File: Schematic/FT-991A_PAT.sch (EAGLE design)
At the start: 51 parts, among them Q1 PE4259, Q10 PE4259, Q2 MC78L09ABDR2GOSCT, Q3 SN74AHC-OR, Q4 PE4259, Q5 NCP553, Q6 PE4259, Q7 J310, Q8 5086, Q9 PE4259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

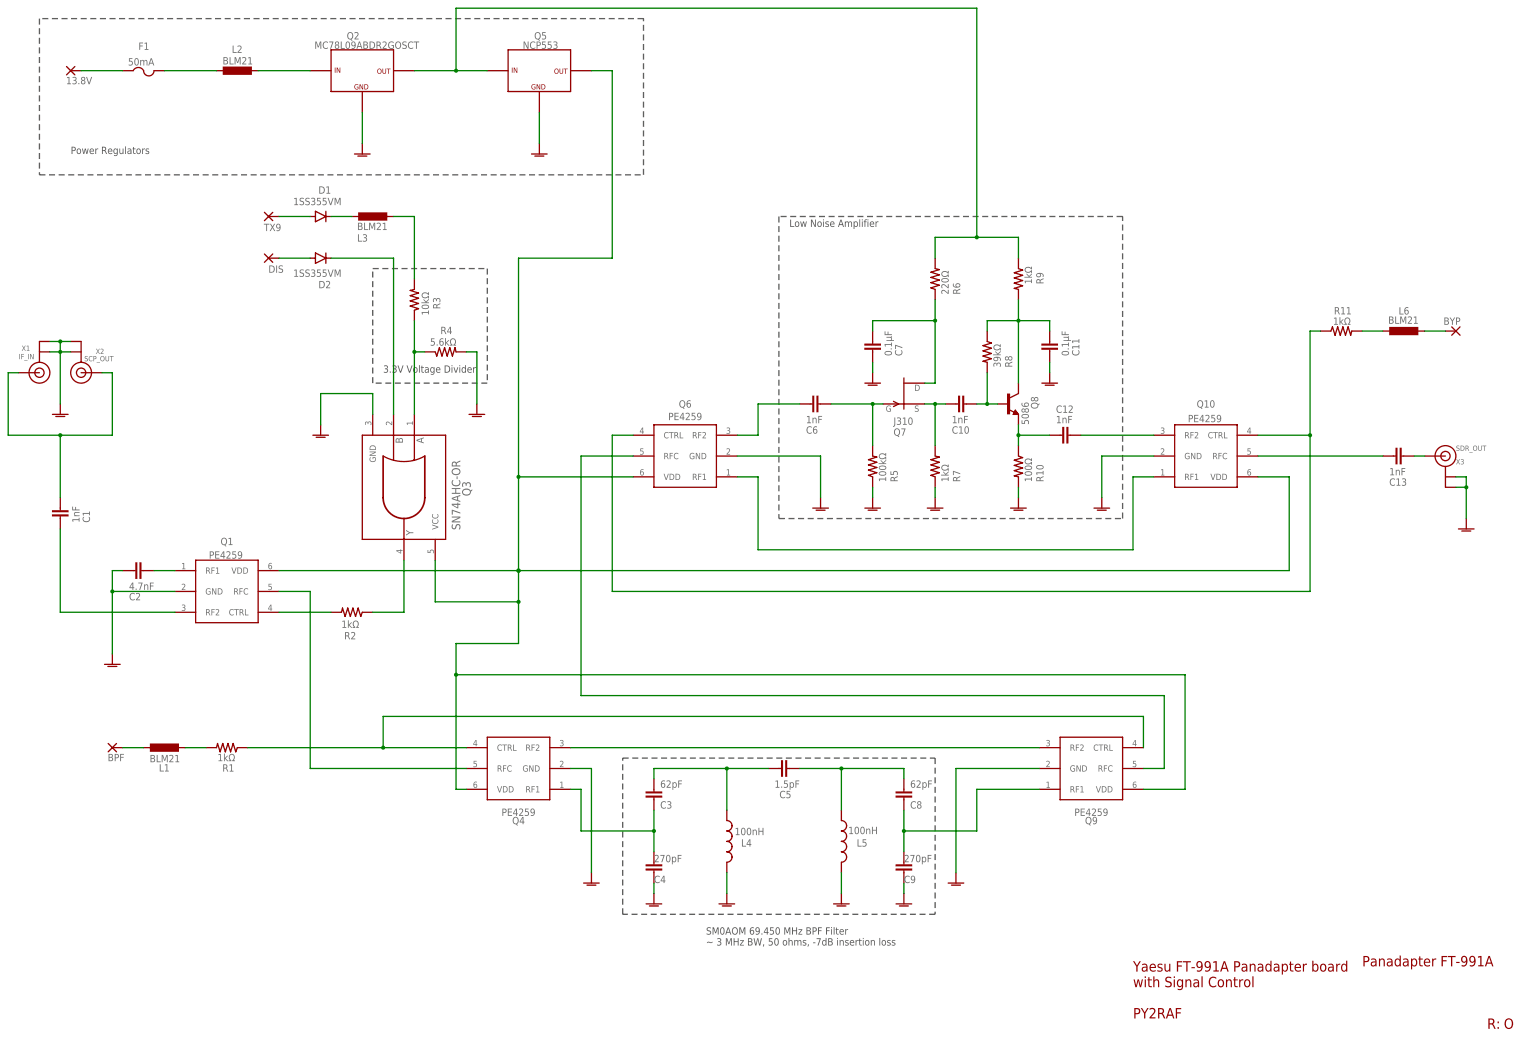
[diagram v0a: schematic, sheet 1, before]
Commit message: Starring: Revision P, Full Version
* Changed RF switch layout - now IF input uses the RF switch's `RFC`
  port instead of RF2 - It seems that the PE4259's `RF{N}` port gets in
  a grounded state instead of just reflecting out the data when the port
  is not selected/active
* Got rid of the "Grounding" in RF1 port; that's not necessary
  because... Above
* Because of that... One less component (the 4.7 nF C2 cap)
* Updated BOM to reflect capacitor removal - also reorganized it
* Few component routing/placement for better ground plane rastnest
* Updated Bandpass .ASC file for use with LTSpice; reflects SM0AOM
  filter, with new values
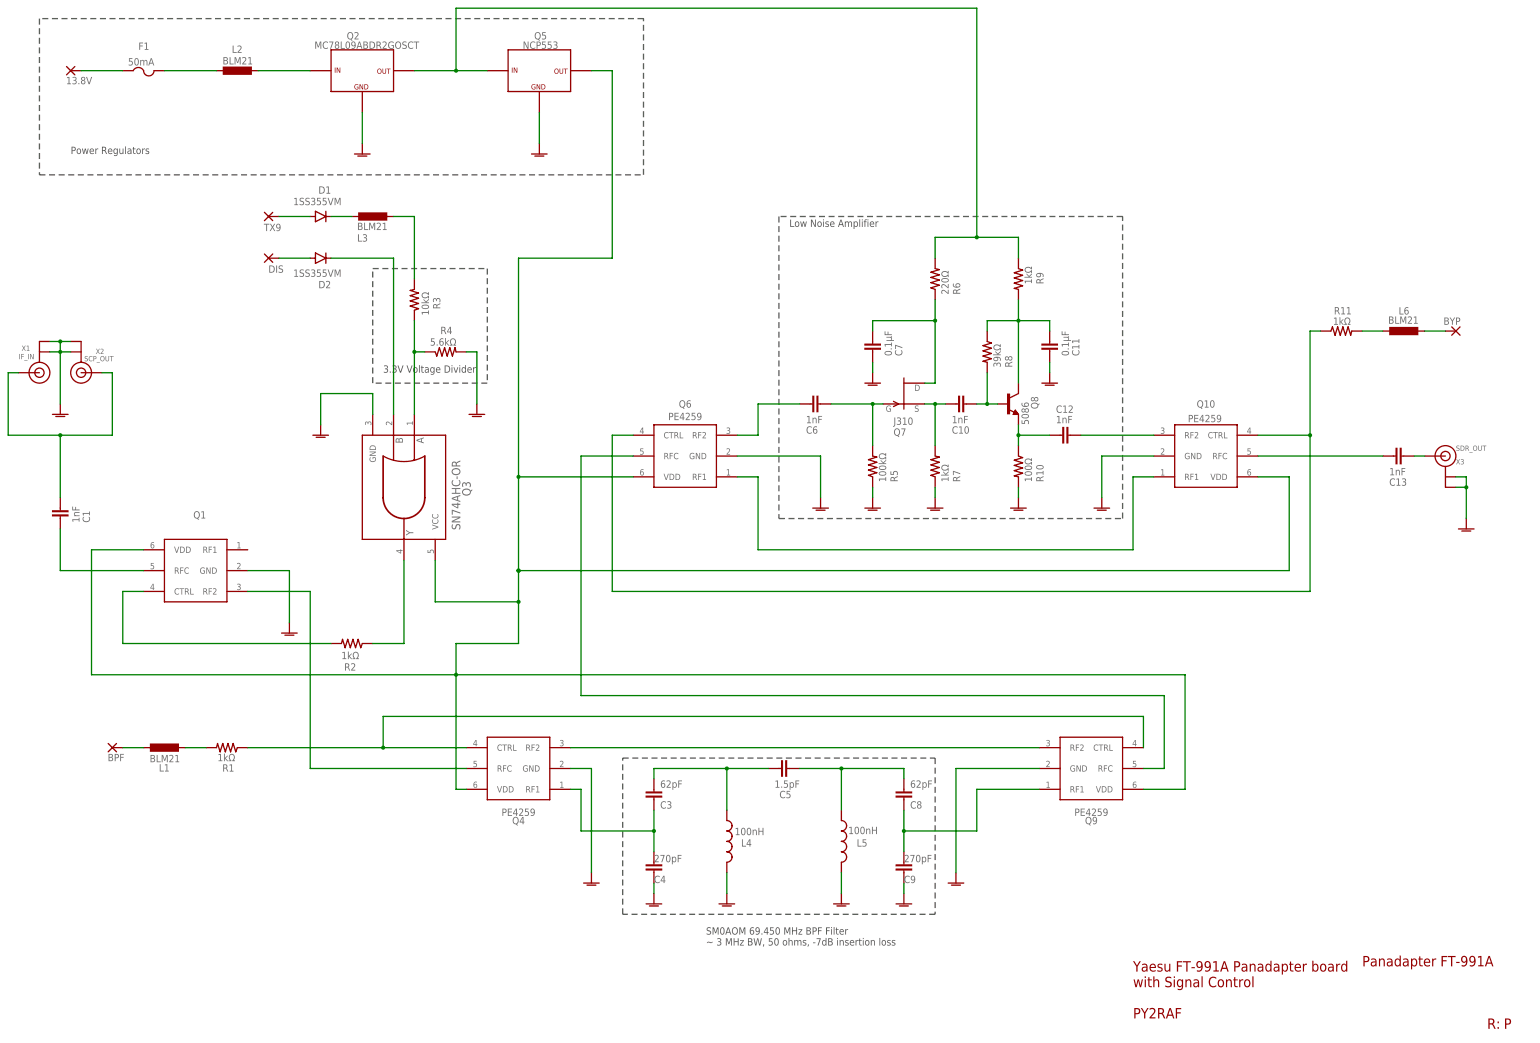
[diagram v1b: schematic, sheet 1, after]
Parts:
- removed C2: 4.7nF, rcl:C-EUC3216
- Q1: value PE4259 -> (none)
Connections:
- removed net N$21: C2.2, Q1.RF1
- net GNDA: no longer C2.1
- net N$24: now also Q1.RFC; no longer Q1.RF2
- net N$47: now also Q1.RF2; no longer Q1.RFC
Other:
- moved on the sheet: Q1, R2

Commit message: Added test points
Added test points for voltage and RF switch lines.
Updated board, schematics and gerbers to reflect the change.
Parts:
- added TP1, TP2, TP3, TP4: TPB1,27, testpad:TPB1,27
- added TP5: BPF, testpad:TPB1,27
- C3, C8: value 62pF -> 56pF
- Q1: value (none) -> PE4259
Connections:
- net N$19: now also TP3.TP
- net N$40: now also TP4.TP
- net N$46: now also TP5.TP
- net VCC: now also TP1.TP
- net VDD: now also TP2.TP
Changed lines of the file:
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@@
 <part name="Q2" library="aarf" deviceset="MC78L" device="" technology="09ABDR2GOSCT"/>
 <part name="C5" library="rcl" library_urn="urn:adsk.eagle:library:334" deviceset="C-EU" device="C0603" package3d_urn="urn:adsk.eagle:package:23616/2" value="1.5pF"/>
-<part name="C8" library="rcl" library_urn="urn:adsk.eagle:library:334" deviceset="C-EU" device="C0805" package3d_urn="urn:adsk.eagle:package:23617/2" value="62pF"/>
+<part name="C8" library="rcl" library_urn="urn:adsk.eagle:library:334" deviceset="C-EU" device="C0805" package3d_urn="urn:adsk.eagle:package:23617/2" value="56pF"/>
 <part name="C4" library="aarf" deviceset="SQCB-1111" device="" value="270pF"/>
 <part name="C9" library="aarf" deviceset="SQCB-1111" device="" value="270pF"/>
 <part name="L4" library="aarf" deviceset="AIAC-1812" device="" value="100nH"/>
 <part name="L5" library="aarf" deviceset="AIAC-1812" device="" value="100nH"/>
-<part name="C3" library="rcl" library_urn="urn:adsk.eagle:library:334" deviceset="C-EU" device="C0805" package3d_urn="urn:adsk.eagle:package:23617/2" value="62pF"/>
-<part name="Q1" library="aarf" deviceset="PE4259" device=""/>
+<part name="C3" library="rcl" library_urn="urn:adsk.eagle:library:334" deviceset="C-EU" device="C0805" package3d_urn="urn:adsk.eagle:package:23617/2" value="56pF"/>
+<part name="Q1" library="aarf" deviceset="PE4259" device="" value="PE4259"/>
+<part name="TP1" library="testpad" library_urn="urn:adsk.eagle:library:385" deviceset="TP" device="B1,27" package3d_urn="urn:adsk.eagle:package:27944/1"/>
+<part name="TP2" library="testpad" library_urn="urn:adsk.eagle:library:385" deviceset="TP" device="B1,27" package3d_urn="urn:adsk.eagle:package:27944/1"/>
+<part name="TP3" library="testpad" library_urn="urn:adsk.eagle:library:385" deviceset="TP" device="B1,27" package3d_urn="urn:adsk.eagle:package:27944/1"/>
+<part name="TP4" library="testpad" library_urn="urn:adsk.eagle:library:385" deviceset="TP" device="B1,27" package3d_urn="urn:adsk.eagle:package:27944/1"/>
+<part name="TP5" library="testpad" library_urn="urn:adsk.eagle:library:385" deviceset="TP" device="B1,27" package3d_urn="urn:adsk.eagle:package:27944/1" value="BPF"/>
 </parts>
 <sheets>
@@
 </instance>
 <instance part="Q1" gate="G$1" x="60.96" y="116.84" smashed="yes" rot="MR0">
-<attribute name="NAME" x="63.5" y="129.54" size="1.778" layer="95" rot="MR0"/>
-<attribute name="VALUE" x="63.5" y="127" size="1.778" layer="96" rot="MR0"/>
+<attribute name="NAME" x="63.5" y="104.14" size="1.778" layer="95" rot="MR0"/>
+<attribute name="VALUE" x="66.04" y="106.68" size="1.778" layer="96" rot="MR0"/>
+</instance>
+<instance part="TP1" gate="G$1" x="124.46" y="223.52" smashed="yes" rot="R180">
+<attribute name="NAME" x="125.73" y="222.25" size="1.778" layer="95" rot="R180"/>
+<attribute name="TP_SIGNAL_NAME" x="123.19" y="224.79" size="1.778" layer="97" rot="R180"/>
+</instance>
+<instance part="TP2" gate="G$1" x="177.8" y="228.6" smashed="yes" rot="R270">
+<attribute name="NAME" x="179.07" y="229.87" size="1.778" layer="95" rot="R270"/>
+<attribute name="TP_SIGNAL_NAME" x="176.53" y="227.33" size="1.778" layer="97" rot="R270"/>
+</instance>
+<instance part="TP3" gate="G$1" x="71.12" y="106.68" smashed="yes">
+<attribute name="NAME" x="69.85" y="107.95" size="1.778" layer="95"/>
+<attribute name="TP_SIGNAL_NAME" x="72.39" y="105.41" size="1.778" layer="97"/>
+</instance>
+<instance part="TP4" gate="G$1" x="248.92" y="104.14" smashed="yes" rot="R180">
+<attribute name="NAME" x="250.19" y="102.87" size="1.778" layer="95" rot="R180"/>
+<attribute name="TP_SIGNAL_NAME" x="247.65" y="105.41" size="1.778" layer="97" rot="R180"/>
+</instance>
+<instance part="TP5" gate="G$1" x="81.28" y="63.5" smashed="yes" rot="R180">
+<attribute name="NAME" x="82.55" y="62.23" size="1.778" layer="95" rot="R180"/>
+<attribute name="TP_SIGNAL_NAME" x="80.01" y="64.77" size="1.778" layer="97" rot="R180"/>
 </instance>
 </instances>
@@
 <wire x1="124.46" y1="254" x2="124.46" y2="238.76" width="0.1524" layer="91"/>
 <junction x="124.46" y="238.76"/>
+<pinref part="TP1" gate="G$1" pin="TP"/>
+<wire x1="124.46" y1="226.06" x2="124.46" y2="238.76" width="0.1524" layer="91"/>
 </segment>
 </net>
@@
 <wire x1="124.46" y1="91.44" x2="124.46" y2="63.5" width="0.1524" layer="91"/>
 <wire x1="124.46" y1="99.06" x2="139.7" y2="99.06" width="0.1524" layer="91"/>
-<wire x1="162.56" y1="238.76" x2="162.56" y2="193.04" width="0.1524" layer="91"/>
+<wire x1="162.56" y1="238.76" x2="162.56" y2="228.6" width="0.1524" layer="91"/>
 <pinref part="Q6" gate="G$1" pin="VDD"/>
+<wire x1="162.56" y1="228.6" x2="162.56" y2="193.04" width="0.1524" layer="91"/>
 <wire x1="167.64" y1="139.7" x2="139.7" y2="139.7" width="0.1524" layer="91"/>
 <junction x="139.7" y="139.7"/>
@@
 <pinref part="Q1" gate="G$1" pin="VDD"/>
 <wire x1="35.56" y1="121.92" x2="48.26" y2="121.92" width="0.1524" layer="91"/>
+<pinref part="TP2" gate="G$1" pin="TP"/>
+<wire x1="175.26" y1="228.6" x2="162.56" y2="228.6" width="0.1524" layer="91"/>
+<junction x="162.56" y="228.6"/>
 </segment>
 </net>
@@
 <wire x1="332.74" y1="149.86" x2="332.74" y2="175.26" width="0.1524" layer="91"/>
 <wire x1="332.74" y1="149.86" x2="332.74" y2="111.76" width="0.1524" layer="91"/>
-<wire x1="332.74" y1="111.76" x2="162.56" y2="111.76" width="0.1524" layer="91"/>
+<wire x1="332.74" y1="111.76" x2="248.92" y2="111.76" width="0.1524" layer="91"/>
 <junction x="332.74" y="149.86"/>
 <pinref part="Q6" gate="G$1" pin="CTRL"/>
+<wire x1="248.92" y1="111.76" x2="162.56" y2="111.76" width="0.1524" layer="91"/>
 <wire x1="162.56" y1="111.76" x2="162.56" y2="149.86" width="0.1524" layer="91"/>
 <wire x1="162.56" y1="149.86" x2="167.64" y2="149.86" width="0.1524" layer="91"/>
+<pinref part="TP4" gate="G$1" pin="TP"/>
+<wire x1="248.92" y1="106.68" x2="248.92" y2="111.76" width="0.1524" layer="91"/>
+<junction x="248.92" y="111.76"/>
 </segment>
 </net>
@@
 <wire x1="127" y1="73.66" x2="106.68" y2="73.66" width="0.1524" layer="91"/>
 <pinref part="R1" gate="G$1" pin="1"/>
-<wire x1="106.68" y1="73.66" x2="73.66" y2="73.66" width="0.1524" layer="91"/>
+<wire x1="106.68" y1="73.66" x2="81.28" y2="73.66" width="0.1524" layer="91"/>
+<wire x1="81.28" y1="73.66" x2="73.66" y2="73.66" width="0.1524" layer="91"/>
 <wire x1="106.68" y1="73.66" x2="106.68" y2="81.28" width="0.1524" layer="91"/>
 <junction x="106.68" y="73.66"/>
@@
 <wire x1="292.1" y1="73.66" x2="292.1" y2="81.28" width="0.1524" layer="91"/>
 <wire x1="292.1" y1="81.28" x2="106.68" y2="81.28" width="0.1524" layer="91"/>
+<pinref part="TP5" gate="G$1" pin="TP"/>
+<wire x1="81.28" y1="66.04" x2="81.28" y2="73.66" width="0.1524" layer="91"/>
+<junction x="81.28" y="73.66"/>
 </segment>
 </net>
@@
 <segment>
 <pinref part="R2" gate="G$1" pin="2"/>
-<wire x1="93.98" y1="99.06" x2="43.18" y2="99.06" width="0.1524" layer="91"/>
+<wire x1="93.98" y1="99.06" x2="71.12" y2="99.06" width="0.1524" layer="91"/>
+<wire x1="71.12" y1="99.06" x2="43.18" y2="99.06" width="0.1524" layer="91"/>
 <wire x1="43.18" y1="99.06" x2="43.18" y2="111.76" width="0.1524" layer="91"/>
 <pinref part="Q1" gate="G$1" pin="CTRL"/>
 <wire x1="43.18" y1="111.76" x2="48.26" y2="111.76" width="0.1524" layer="91"/>
-</segment>
-</net>
+<pinref part="TP3" gate="G$1" pin="TP"/>
+<wire x1="71.12" y1="104.14" x2="71.12" y2="99.06" width="0.1524" layer="91"/>
+<junction x="71.12" y="99.06"/>
+</segment>
+</net>
